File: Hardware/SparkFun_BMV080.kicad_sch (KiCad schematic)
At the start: 23 parts, among them J1 Qwiic_RA, J2 Qwiic_RA, J3 Conn_01x06, J4 Conn_01x01, U1 BMV080

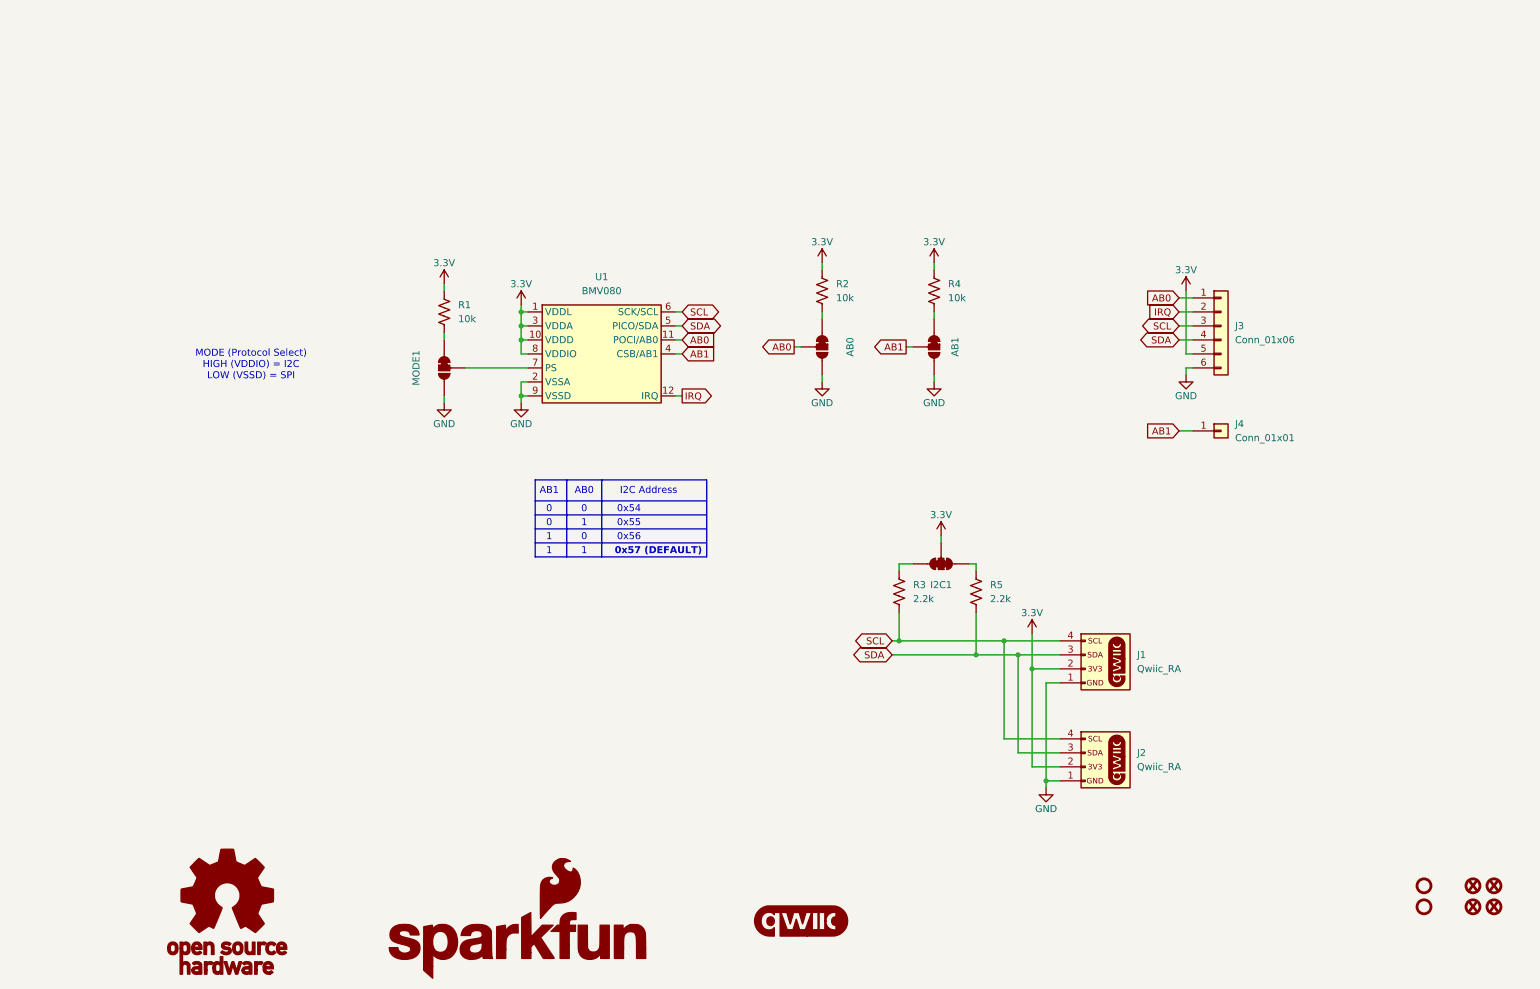
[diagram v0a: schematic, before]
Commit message: schematic cleanup and reroute
-added section divider lines and section titles
-jumper reference and naming corrected, rotated text in sch to all horizontal
-added company and defined by:
-rearranged part name and value texts for calrity
-moved logos in sch to proper location
-moved to vertical qwiic connector
-added decoupling caps
-added exposed copper for potential heat sink
-added silk to jumpers
-added qwiic logo to silk
-added version v01 to bottom copper
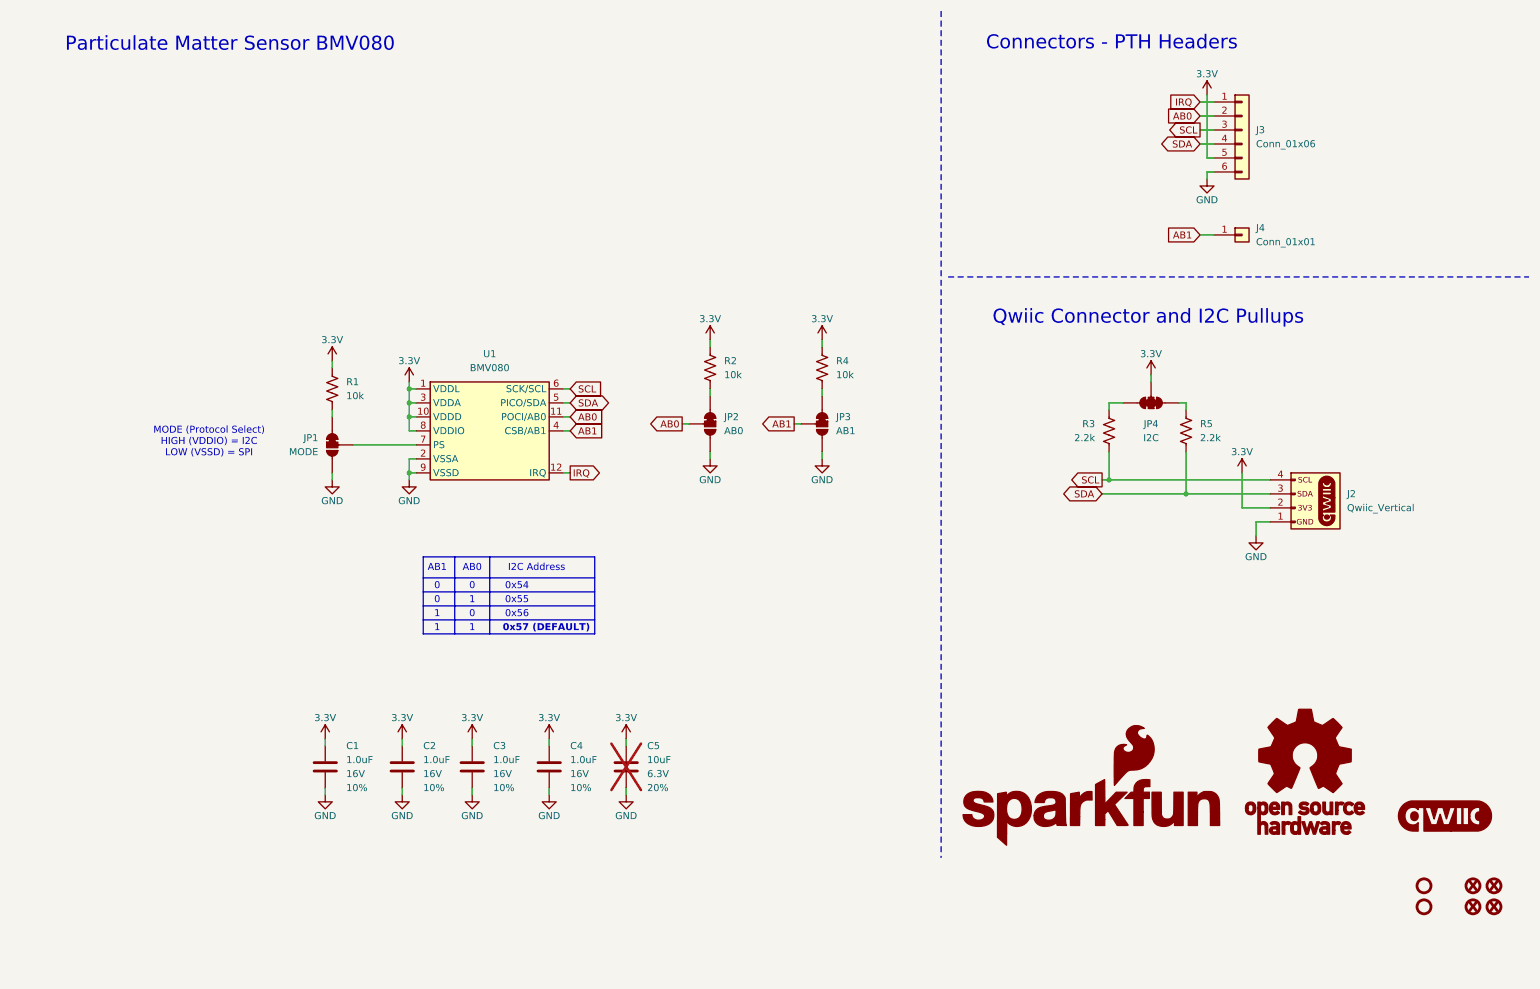
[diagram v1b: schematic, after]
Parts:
- removed J1, J2: Qwiic_RA, SparkFun-Connector:JST_SMD_1.0mm-4_RA, symbol SparkFun-Connector:Qwiic_Right_Angle
- added C1, C2, C3, C4: 1.0uF, SparkFun-Capacitor:C_0402_1005Metric, symbol SparkFun-Capacitor:1.0uF_0402_16V_10%
- added C5: 10uF, SparkFun-Capacitor:C_0603_1608Metric, symbol SparkFun-Capacitor:10uF_0603_6.3V_20%
- added J2: Qwiic_Vertical, SparkFun-Connector:JST_SMD_1.0mm-4_Vertical, symbol SparkFun-Connector:Qwiic_Vertical
- JP1: renamed from MODE1; value ~ -> MODE
- JP2: renamed from AB0; value ~ -> AB0
- JP3: renamed from AB1; value ~ -> AB1
- JP4: renamed from I2C1; value ~ -> I2C
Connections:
- net 3.3V: now also C1.1, C2.1, C3.1, C4.1, C5.1, J2.2 (Pin_2)
- net AB0: now also J3.2 (Pin_2); no longer J3.1 (Pin_1)
- net GND: now also C1.2, C2.2, C3.2, C4.2, C5.2, J2.1 (Pin_1)
- net IRQ: now also J3.1 (Pin_1); no longer J3.2 (Pin_2)
- net SCL: now also J2.4 (Pin_4)
- net SDA: now also J2.3 (Pin_3)
- new net: J2.NC1 (NC), J2.NC2 (NC)
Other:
- note added: "Connectors - PTH Headers"
- note added: "Particulate Matter Sensor BMV080"
- note added: "Qwiic Connector and I2C Pullups"
- company: (none) -> SparkFun Electronics
- moved on the sheet: J3, J4, JP1, JP2, JP3, JP4, R1, R2, R3, R4, R5, U1

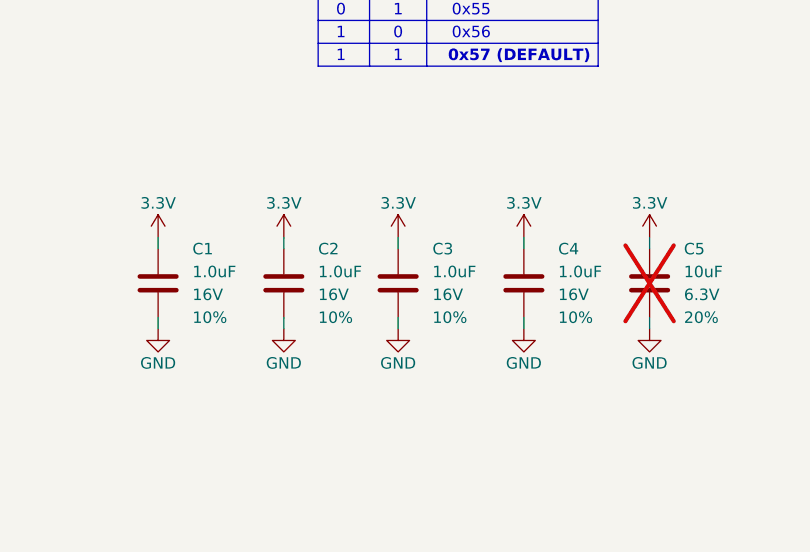
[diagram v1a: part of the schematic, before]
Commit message: changed bypass caps to larger value of 2.2uF
-bypass caps bumped up from 1.0uF to 2.2uF as per recommended in datasheet
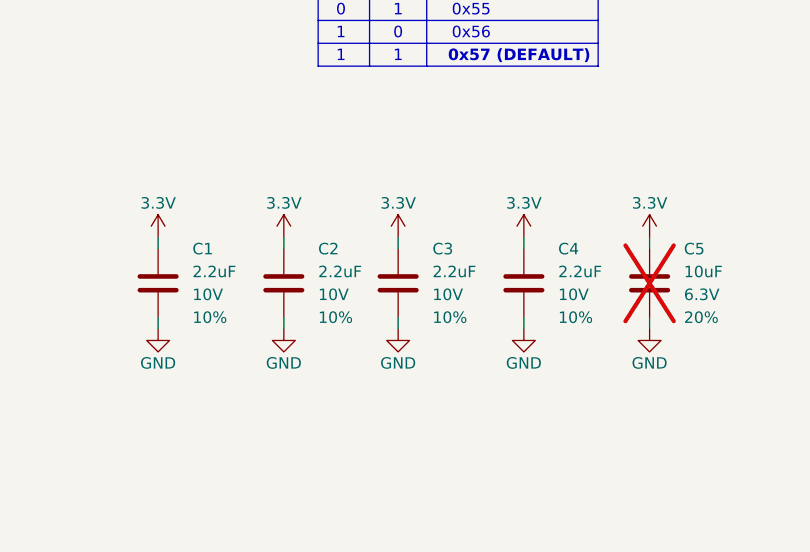
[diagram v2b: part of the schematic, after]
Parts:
- removed C1, C2, C3, C4: 1.0uF, SparkFun-Capacitor:C_0402_1005Metric, symbol SparkFun-Capacitor:1.0uF_0402_16V_10%
- added C1, C2, C3, C4: 2.2uF, SparkFun-Capacitor:C_0402_1005Metric, symbol SparkFun-Capacitor:2.2uF_0402_10V_10%
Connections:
- net 3.3V: now also C1.1, C2.1, C3.1, C4.1
- net GND: now also C1.2, C2.2, C3.2, C4.2

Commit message: jumpers to no silk outline and prod_id on ic
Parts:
- removed JP1: MODE, SparkFun-Jumper:Jumper_3_NC-1_Trace, symbol SparkFun-Jumper:SolderJumper_3_Bridged12
- removed JP2: AB0, SparkFun-Jumper:Jumper_3_NC-1_Trace, symbol SparkFun-Jumper:SolderJumper_3_Bridged12
- removed JP3: AB1, SparkFun-Jumper:Jumper_3_NC-1_Trace, symbol SparkFun-Jumper:SolderJumper_3_Bridged12
- removed JP4: I2C, SparkFun-Jumper:Jumper_3_NC-2_Trace, symbol SparkFun-Jumper:SolderJumper_3_Bridged123
- added JP1: MODE, SparkFun-Jumper:Jumper_3_NC-1_Trace_NoSilk, symbol SparkFun-Jumper:SolderJumper_3_Bridged12_No_Silk
- added JP2: AB0, SparkFun-Jumper:Jumper_3_NC-1_Trace_NoSilk, symbol SparkFun-Jumper:SolderJumper_3_Bridged12_No_Silk
- added JP3: AB1, SparkFun-Jumper:Jumper_3_NC-1_Trace_NoSilk, symbol SparkFun-Jumper:SolderJumper_3_Bridged12_No_Silk
- added JP4: I2C, SparkFun-Jumper:Jumper_3_NC-2_Trace_NoSilk, symbol SparkFun-Jumper:SolderJumper_3_Bridged123_No_Silk
- U1: PROD_ID IC- -> IC-22926
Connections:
- net 3.3V: now also JP4.2 (C)
- net AB0: now also JP2.2 (C)
- net AB1: now also JP3.2 (C)
- net GND: now also JP1.3 (B), JP2.3 (B), JP3.3 (B)
- net at R1.2: now also JP1.1 (A)
- net at U1.7 (PS): now also JP1.2 (C)
- net at R4.2: now also JP3.1 (A)
- net at R3.2: now also JP4.3 (B)
- net at R2.2: now also JP2.1 (A)
- net at R5.2: now also JP4.1 (A)
